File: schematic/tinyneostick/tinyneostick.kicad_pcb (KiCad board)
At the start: 2 copper layers, 57 x 7.8 mm, 18 parts, among them J1 Conn_01x03, J2 Conn_01x03

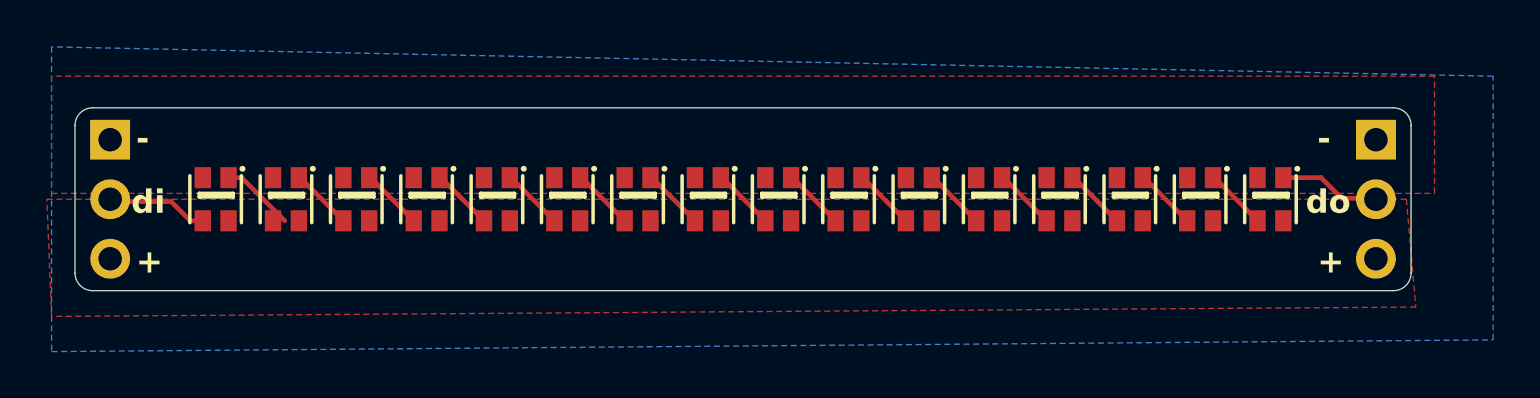
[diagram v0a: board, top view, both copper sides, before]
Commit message: smd version, 48mm x 7.8mm, cannot be PCBAd by JLC tho
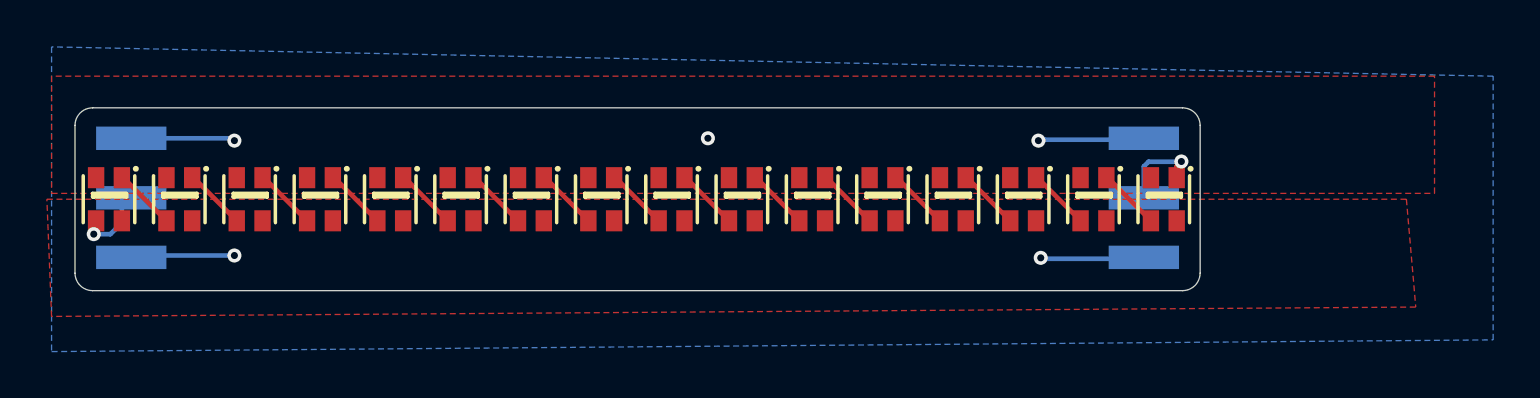
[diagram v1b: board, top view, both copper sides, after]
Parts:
- J1, J2: footprint Connector_PinHeader_2.54mm:PinHeader_1x03_P2.54mm_Vertical -> todbot_stuff:Pins_1x03_P2.54mm_Horizontal_SMT
- moved J2 10.2 mm to (68.3, 21.5)
- moved LED10 4.55 mm to (51.1, 21.5)
- moved LED11 4.55 mm to (54.1, 21.5)
- moved LED12 4.55 mm to (57.1, 21.5)
- moved LED13 4.55 mm to (60.1, 21.5)
- moved LED14 4.55 mm to (63.1, 21.5)
- moved LED3 4.55 mm to (30.1, 21.5)
- moved LED4 4.55 mm to (33.1, 21.5)
- moved LED5 4.55 mm to (36.1, 21.5)
- moved LED6 4.55 mm to (39.1, 21.5)
- moved LED7 4.55 mm to (42.1, 21.5)
- moved LED8 4.55 mm to (45.1, 21.5)
- moved LED9 4.55 mm to (48.1, 21.5)
- moved LED1 4.55 mm to (24.1, 21.5)
- moved LED2 4.55 mm to (27.1, 21.5)
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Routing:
- net GND: track 0.00 -> 9.79 mm, vias 0 -> 3
- net VDD: track 0.00 -> 9.62 mm, vias 0 -> 2
- net /DI: track 4.29 -> 3.15 mm, vias 0 -> 1
- net /DO: track 4.31 -> 3.80 mm, vias 0 -> 1
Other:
- board size 57 x 7.8 mm -> 48 x 7.8 mm
- board text removed: "di"
- board text removed: "do"

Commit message: 48mm x 10mm version
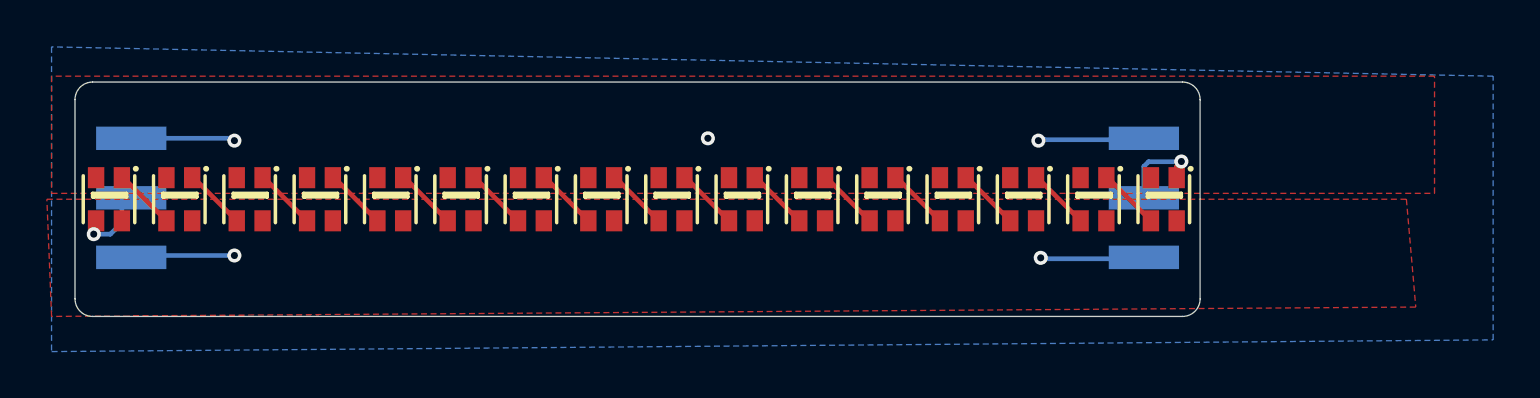
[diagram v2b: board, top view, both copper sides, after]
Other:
- board size 48 x 7.8 mm -> 48 x 10 mm
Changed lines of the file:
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@@
 	)
 	(gr_line
-		(start 70.7 18.35)
-		(end 70.7 24.65)
+		(start 70.7 17.25)
+		(end 70.7 25.75)
+		(stroke
+			(width 0.05)
+			(type default)
+		)
+		(layer "Edge.Cuts")
+	)
+	(gr_line
+		(start 23.45 16.5)
+		(end 69.95 16.5)
 		(stroke
 			(width 0.05)
@@
 	)
 	(gr_arc
-		(start 70.7 24.65)
-		(mid 70.48033 25.18033)
-		(end 69.95 25.4)
+		(start 22.7 17.25)
+		(mid 22.91967 16.71967)
+		(end 23.45 16.5)
 		(stroke
 			(width 0.05)
@@
 	)
 	(gr_line
-		(start 23.45 17.6)
-		(end 69.95 17.6)
+		(start 22.7 25.75)
+		(end 22.7 17.25)
 		(stroke
 			(width 0.05)
@@
 	)
 	(gr_arc
-		(start 69.95 17.6)
-		(mid 70.48033 17.81967)
-		(end 70.7 18.35)
+		(start 70.7 25.75)
+		(mid 70.48033 26.28033)
+		(end 69.95 26.5)
+		(stroke
+			(width 0.05)
+			(type default)
+		)
+		(layer "Edge.Cuts")
+	)
+	(gr_arc
+		(start 69.95 16.5)
+		(mid 70.48033 16.71967)
+		(end 70.7 17.25)
 		(stroke
 			(width 0.05)
@@
 	)
 	(gr_line
-		(start 22.7 24.65)
-		(end 22.7 18.35)
-		(stroke
-			(width 0.05)
-			(type default)
-		)
-		(layer "Edge.Cuts")
-	)
-	(gr_line
-		(start 69.95 25.4)
-		(end 23.45 25.4)
+		(start 69.95 26.5)
+		(end 23.45 26.5)
 		(stroke
 			(width 0.05)
@@
 	)
 	(gr_arc
-		(start 22.7 18.35)
-		(mid 22.91967 17.81967)
-		(end 23.45 17.6)
+		(start 23.45 26.5)
+		(mid 22.91967 26.28033)
+		(end 22.7 25.75)
 		(stroke
 			(width 0.05)
-			(type default)
-		)
-		(layer "Edge.Cuts")
-	)
-	(gr_arc
-		(start 23.45 25.4)
-		(mid 22.91967 25.18033)
-		(end 22.7 24.65)
-		(stroke
-			(width 0.05)

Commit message: small fixes
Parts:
- J1, J2: footprint todbot_stuff:Pins_1x03_P2.54mm_Horizontal_SMT -> todbot_stuff:Pins_1x03_P2.54mm_Horizontal_SMT_bigger
- moved J1 0.10 mm to (25.1, 21.5)
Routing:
- net /DO: track 3.80 -> 21.7 mm
- net /DI: track 3.15 -> 20.1 mm
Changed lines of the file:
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@@
 		)
 	)
-	(footprint "todbot_stuff:Pins_1x03_P2.54mm_Horizontal_SMT"
+	(footprint "todbot_stuff:Pins_1x03_P2.54mm_Horizontal_SMT_bigger"
 		(layer "B.Cu")
 		(at 68.35 21.5 180)
@@
 		(attr through_hole exclude_from_bom)
 		(fp_line
-			(start 1.8 4.4)
-			(end -1.7 4.4)
+			(start 2 4.4)
+			(end -1.9 4.4)
 			(stroke
 				(width 0.05)
@@
 		)
 		(fp_line
-			(start 1.8 -4.25)
-			(end 1.8 4.4)
+			(start 2 -4.25)
+			(end 2 4.4)
 			(stroke
 				(width 0.05)
@@
 		)
 		(fp_line
-			(start -1.7 4.4)
-			(end -1.7 -4.25)
+			(start -1.9 4.4)
+			(end -1.9 -4.25)
 			(stroke
 				(width 0.05)
@@
 		)
 		(fp_line
-			(start -1.7 -4.25)
-			(end 1.8 -4.25)
+			(start -1.9 -4.25)
+			(end 2 -4.25)
 			(stroke
 				(width 0.05)
@@
 		(pad "1" smd rect
 			(at 0.05 2.6 180)
-			(size 3 1)
+			(size 3.5 1.2)
 			(layers "B.Cu" "B.Mask" "B.Paste")
 			(net 1 "GND")
@@
 		(pad "2" smd rect
 			(at 0.05 0.06 90)
-			(size 1 3)
+			(size 1.2 3.5)
 			(layers "B.Cu" "B.Mask" "B.Paste")
 			(net 5 "/DO")
@@
 		(pad "3" smd rect
 			(at 0.05 -2.48 90)
-			(size 1 3)
+			(size 1.2 3.5)
 			(layers "B.Cu" "B.Mask" "B.Paste")
 			(net 2 "VDD")
@@
 		)
 	)
-	(footprint "todbot_stuff:Pins_1x03_P2.54mm_Horizontal_SMT"
-		(layer "B.Cu")
-		(at 25.15 21.5 180)
+	(footprint "todbot_stuff:Pins_1x03_P2.54mm_Horizontal_SMT_bigger"
+		(layer "B.Cu")
+		(at 25.05 21.5 180)
 		(descr "SMT angled pins, 1x03, 2.54mm pitch, 5.84mm pin length")
 		(tags "SMT angled pins 1x03 2.54mm single row")
@@
 		(attr through_hole exclude_from_bom)
 		(fp_line
-			(start 1.8 4.4)
-			(end -1.7 4.4)
+			(start 2 4.4)
+			(end -1.9 4.4)
 			(stroke
 				(width 0.05)
@@
 		)
 		(fp_line
-			(start 1.8 -4.25)
-			(end 1.8 4.4)
+			(start 2 -4.25)
+			(end 2 4.4)
 			(stroke
 				(width 0.05)
@@
 		)
 		(fp_line
-			(start -1.7 4.4)
-			(end -1.7 -4.25)
+			(start -1.9 4.4)
+			(end -1.9 -4.25)
 			(stroke
 				(width 0.05)
@@
 		)
 		(fp_line
-			(start -1.7 -4.25)
-			(end 1.8 -4.25)
+			(start -1.9 -4.25)
+			(end 2 -4.25)
 			(stroke
 				(width 0.05)
@@
 		(pad "1" smd rect
 			(at 0.05 2.6 180)
-			(size 3 1)
+			(size 3.5 1.2)
 			(layers "B.Cu" "B.Mask" "B.Paste")
 			(net 1 "GND")
@@
 		(pad "2" smd rect
 			(at 0.05 0.06 90)
-			(size 1 3)
+			(size 1.2 3.5)
 			(layers "B.Cu" "B.Mask" "B.Paste")
 			(net 3 "/DI")
@@
 		(pad "3" smd rect
 			(at 0.05 -2.48 90)
-			(size 1 3)
+			(size 1.2 3.5)
 			(layers "B.Cu" "B.Mask" "B.Paste")
 			(net 2 "VDD")
@@
 	)
 	(gr_text "-"
-		(at 26.9 18.85 0)
+		(at 27.4 18.85 0)
 		(layer "B.SilkS")
 		(effects
@@
 	)
 	(gr_text "+"
-		(at 26.9 23.95 0)
+		(at 27.4 23.95 0)
 		(layer "B.SilkS")
 		(effects
@@
 	)
 	(gr_text "din"
-		(at 26.9 21.3 0)
+		(at 27.4 21.3 0)
 		(layer "B.SilkS")
 		(effects
@@
 	)
 	(segment
-		(start 23.499999 22.990101)
-		(end 23.6 22.8901)
+		(start 31.7 24.8)
+		(end 30.901 25.599)
 		(width 0.2)
 		(layer "F.Cu")
@@
 	)
 	(segment
-		(start 23.6 22.8901)
+		(start 30.901 25.599)
+		(end 24.299 25.599)
+		(width 0.2)
+		(layer "F.Cu")
+		(net 3)
+	)
+	(segment
+		(start 24.299 25.599)
+		(end 23.6 24.9)
+		(width 0.2)
+		(layer "F.Cu")
+		(net 3)
+	)
+	(segment
+		(start 23.6 24.9)
 		(end 23.6 22.42)
 		(width 0.2)
@@
 	)
 	(via
-		(at 23.499999 22.990101)
+		(at 31.7 24.8)
 		(size 0.6)
 		(drill 0.3)
@@
 	)
 	(segment
-		(start 23.499999 22.990101)
-		(end 24.209899 22.990101)
+		(start 31.7 22.8)
+		(end 30.34 21.44)
 		(width 0.2)
 		(layer "B.Cu")
@@
 	)
 	(segment
-		(start 24.209899 22.990101)
-		(end 24.7 22.5)
+		(start 31.7 24.8)
+		(end 31.7 22.8)
 		(width 0.2)
 		(layer "B.Cu")
@@
 	)
 	(segment
-		(start 24.7 22.5)
-		(end 24.7 21.365)
+		(start 30.34 21.44)
+		(end 25.4 21.44)
 		(width 0.2)
 		(layer "B.Cu")
@@
 	)
 	(segment
-		(start 69.9 19.889899)
-		(end 69.7 20.089898)
+		(start 69.7 20.58)
+		(end 69.7 19.1)
 		(width 0.2)
 		(layer "F.Cu")
@@
 	)
 	(segment
-		(start 69.7 20.089898)
-		(end 69.7 20.58)
+		(start 60.3 18.2)
+		(end 60.3 19)
 		(width 0.2)
 		(layer "F.Cu")
 		(net 5)
 	)
+	(segment
+		(start 61.2 17.3)
+		(end 60.3 18.2)
+		(width 0.2)
+		(layer "F.Cu")
+		(net 5)
+	)
+	(segment
+		(start 69.7 19.1)
+		(end 67.9 17.3)
+		(width 0.2)
+		(layer "F.Cu")
+		(net 5)
+	)
+	(segment
+		(start 67.9 17.3)
+		(end 61.2 17.3)
+		(width 0.2)
+		(layer "F.Cu")
+		(net 5)
+	)
 	(via
-		(at 69.9 19.889899)
+		(at 60.3 19)
 		(size 0.6)
 		(drill 0.3)
@@
 	)
 	(segment
-		(start 68.3 20.1)
-		(end 68.3 21.44)
+		(start 62.64 21.44)
+		(end 60.3 19.1)
 		(width 0.2)
 		(layer "B.Cu")
@@
 	)
 	(segment
-		(start 69.9 19.889899)
-		(end 69.889896 19.900002)
+		(start 68.1 21.44)
+		(end 62.64 21.44)
 		(width 0.2)
 		(layer "B.Cu")
@@
 	)
 	(segment
-		(start 68.499998 19.900002)
-		(end 68.3 20.1)
-		(width 0.2)
-		(layer "B.Cu")
-		(net 5)
-	)
-	(segment
-		(start 69.889896 19.900002)
-		(end 68.499998 19.900002)
-		(width 0.2)
-		(layer "B.Cu")
+		(start 60.3 19.1)
+		(end 60.3 19)
+		(width 0.2)
+		(layer "B.Cu")
